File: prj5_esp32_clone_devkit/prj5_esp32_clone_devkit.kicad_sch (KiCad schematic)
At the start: 34 parts, among them J1 USB_B_Micro, J2 Conn_01x19_Pin, J3 Conn_01x19_Pin, Q1 MMSS8050-H-TP, Q2 MMSS8050-H-TP, SW1 SW_Push, SW2 SW_Push, U1 CP2102N-A01-GQFN28, U2 AMS1117-3.3

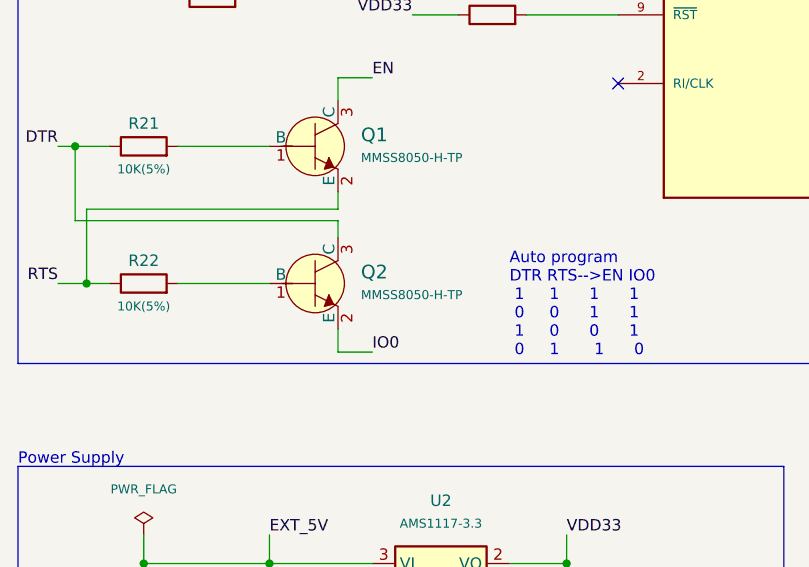
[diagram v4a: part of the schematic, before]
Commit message: Correzione orientamento Q2
Fix: corretto l'orientamento di Q2 nello schematico
Fix: riportata la correzione sul PCB
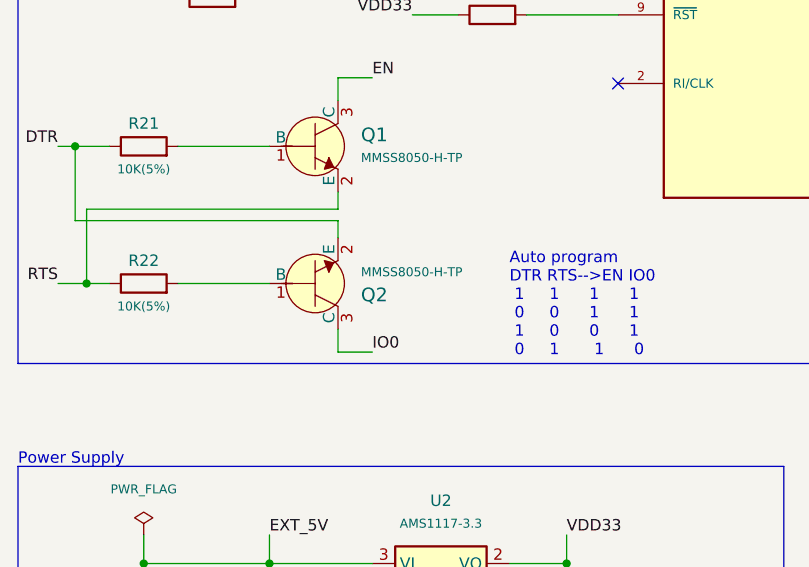
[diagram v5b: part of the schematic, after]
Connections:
- net DTR: now also Q2.2 (E); no longer Q2.3 (C)
- net IO0: now also Q2.3 (C); no longer Q2.2 (E)
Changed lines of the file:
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@@
+    (stroke (width 0) (type default))
+  )
+  (wire (pts (xy 34.29 111.76) (xy 44.45 111.76))
     (stroke (width 0) (type default))
   )
@@
   )
   (wire (pts (xy 222.885 43.18) (xy 226.06 43.18))
-    (stroke (width 0) (type default))
-  )
-  (wire (pts (xy 34.29 111.76) (xy 44.45 111.76))
     (stroke (width 0) (type default))
   )
@@
     )
   )
-  (symbol (lib_id "dk_Transistors-Bipolar-BJT-Single:MMSS8050-H-TP") (at 49.53 111.76 0) (unit 1)
+  (symbol (lib_id "dk_Transistors-Bipolar-BJT-Single:MMSS8050-H-TP") (at 49.53 111.76 0) (mirror x) (unit 1)
     (in_bom yes) (on_board yes) (dnp no)
-    (property "Reference" "Q2" (at 54.61 110.49 0)
+    (property "Reference" "Q2" (at 54.61 113.03 0)
       (effects (font (size 1.524 1.524)) (justify left))
     )
-    (property "Value" "MMSS8050-H-TP" (at 54.61 113.03 0)
+    (property "Value" "MMSS8050-H-TP" (at 54.61 110.49 0)
       (effects (font (size 1 1)) (justify left))
     )
-    (property "Footprint" "digikey-footprints:SOT-23-3" (at 54.61 106.68 0)
-      (effects (font (size 1.524 1.524)) (justify left) hide)
-    )
-    (property "Datasheet" "https://www.mccsemi.com/pdf/Products/MMSS8050(SOT-23).pdf" (at 54.61 104.14 0)
-      (effects (font (size 1.524 1.524)) (justify left) hide)
-    )
-    (property "Digi-Key_PN" "MMSS8050-H-TPMSCT-ND" (at 54.61 101.6 0)
-      (effects (font (size 1.524 1.524)) (justify left) hide)
-    )
-    (property "MPN" "MMSS8050-H-TP" (at 54.61 99.06 0)
-      (effects (font (size 1.524 1.524)) (justify left) hide)
-    )
-    (property "Category" "Discrete Semiconductor Products" (at 54.61 96.52 0)
-      (effects (font (size 1.524 1.524)) (justify left) hide)
-    )
-    (property "Family" "Transistors - Bipolar (BJT) - Single" (at 54.61 93.98 0)
-      (effects (font (size 1.524 1.524)) (justify left) hide)
-    )
-    (property "DK_Datasheet_Link" "https://www.mccsemi.com/pdf/Products/MMSS8050(SOT-23).pdf" (at 54.61 91.44 0)
-      (effects (font (size 1.524 1.524)) (justify left) hide)
-    )
-    (property "DK_Detail_Page" "/product-detail/en/micro-commercial-co/MMSS8050-H-TP/MMSS8050-H-TPMSCT-ND/2825945" (at 54.61 88.9 0)
-      (effects (font (size 1.524 1.524)) (justify left) hide)
-    )
-    (property "Description" "TRANS NPN 25V 1.5A SOT23" (at 54.61 86.36 0)
-      (effects (font (size 1.524 1.524)) (justify left) hide)
-    )
-    (property "Manufacturer" "Micro Commercial Co" (at 54.61 83.82 0)
-      (effects (font (size 1.524 1.524)) (justify left) hide)
-    )
-    (property "Status" "Active" (at 54.61 81.28 0)
-      (effects (font (size 1.524 1.524)) (justify left) hide)
-    )
+    (property "Footprint" "digikey-footprints:SOT-23-3" (at 54.61 116.84 0)
+      (effects (font (size 1.524 1.524)) (justify left) hide)
+    )
+    (property "Datasheet" "https://www.mccsemi.com/pdf/Products/MMSS8050(SOT-23).pdf" (at 54.61 119.38 0)
+      (effects (font (size 1.524 1.524)) (justify left) hide)
+    )
+    (property "Digi-Key_PN" "MMSS8050-H-TPMSCT-ND" (at 54.61 121.92 0)
+      (effects (font (size 1.524 1.524)) (justify left) hide)
+    )
+    (property "MPN" "MMSS8050-H-TP" (at 54.61 124.46 0)
+      (effects (font (size 1.524 1.524)) (justify left) hide)
+    )
+    (property "Category" "Discrete Semiconductor Products" (at 54.61 127 0)
+      (effects (font (size 1.524 1.524)) (justify left) hide)
+    )
+    (property "Family" "Transistors - Bipolar (BJT) - Single" (at 54.61 129.54 0)
+      (effects (font (size 1.524 1.524)) (justify left) hide)
+    )
+    (property "DK_Datasheet_Link" "https://www.mccsemi.com/pdf/Products/MMSS8050(SOT-23).pdf" (at 54.61 132.08 0)
+      (effects (font (size 1.524 1.524)) (justify left) hide)
+    )
+    (property "DK_Detail_Page" "/product-detail/en/micro-commercial-co/MMSS8050-H-TP/MMSS8050-H-TPMSCT-ND/2825945" (at 54.61 134.62 0)
+      (effects (font (size 1.524 1.524)) (justify left) hide)
+    )
+    (property "Description" "TRANS NPN 25V 1.5A SOT23" (at 54.61 137.16 0)
+      (effects (font (size 1.524 1.524)) (justify left) hide)
+    )
+    (property "Manufacturer" "Micro Commercial Co" (at 54.61 139.7 0)
+      (effects (font (size 1.524 1.524)) (justify left) hide)
+    )
+    (property "Status" "Active" (at 54.61 142.24 0)
+      (effects (font (size 1.524 1.524)) (justify left) hide)
+    )
